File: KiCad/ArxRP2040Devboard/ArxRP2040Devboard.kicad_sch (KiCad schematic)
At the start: 14 parts, among them J1 USB_C_Receptacle_USB2.0_14P, U2 RP2040

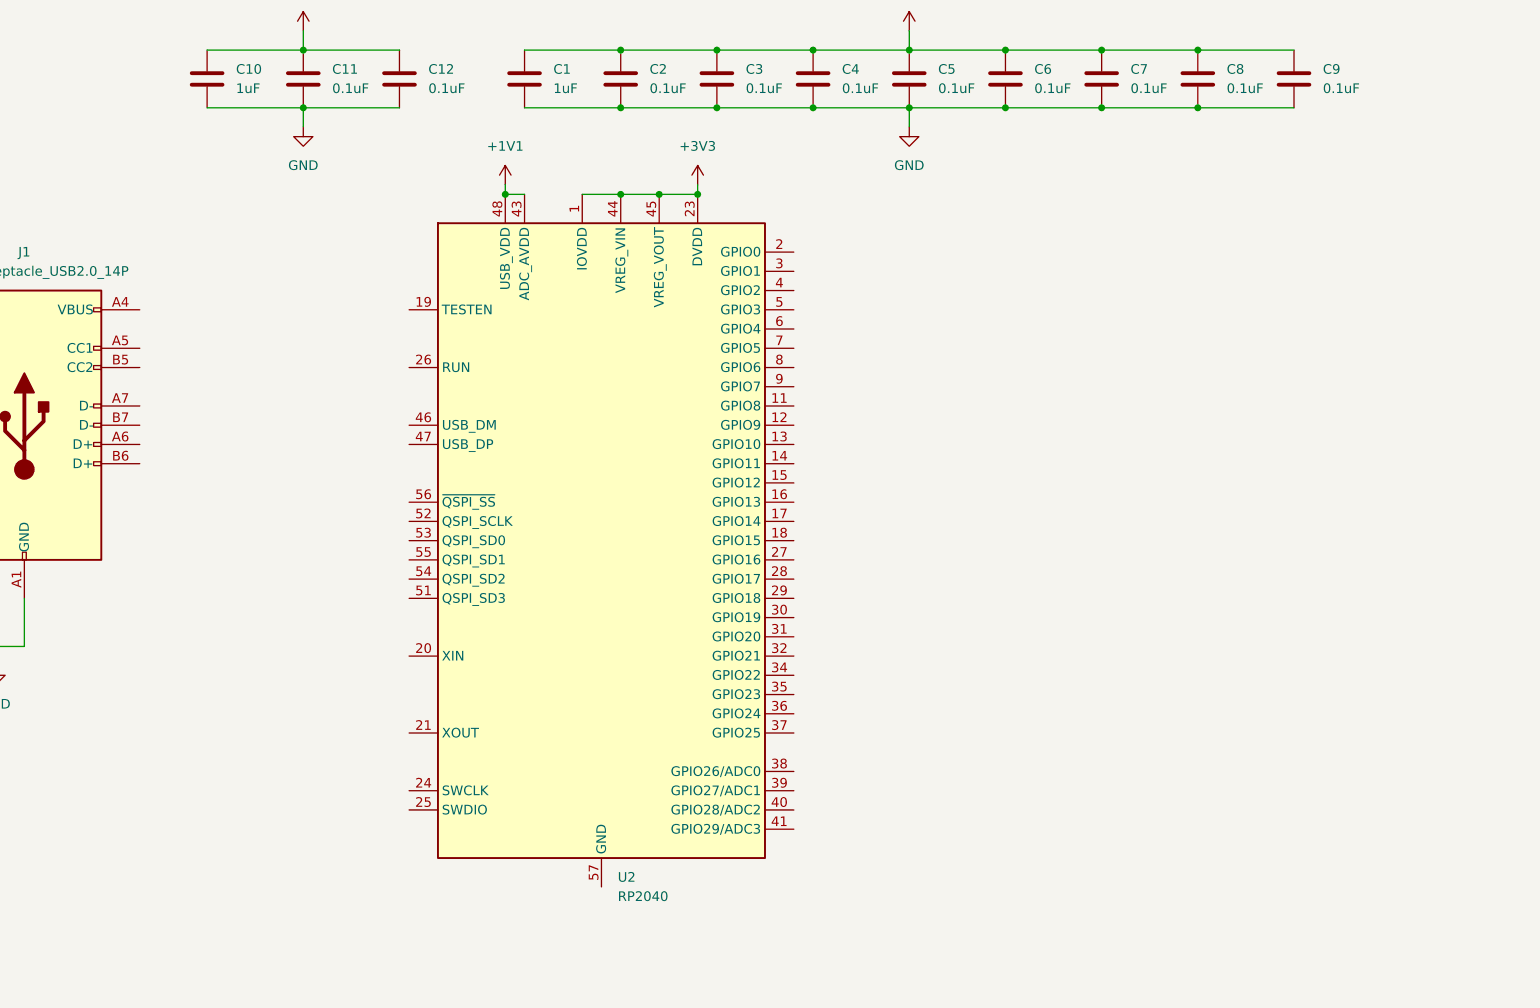
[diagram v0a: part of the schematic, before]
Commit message: More connections
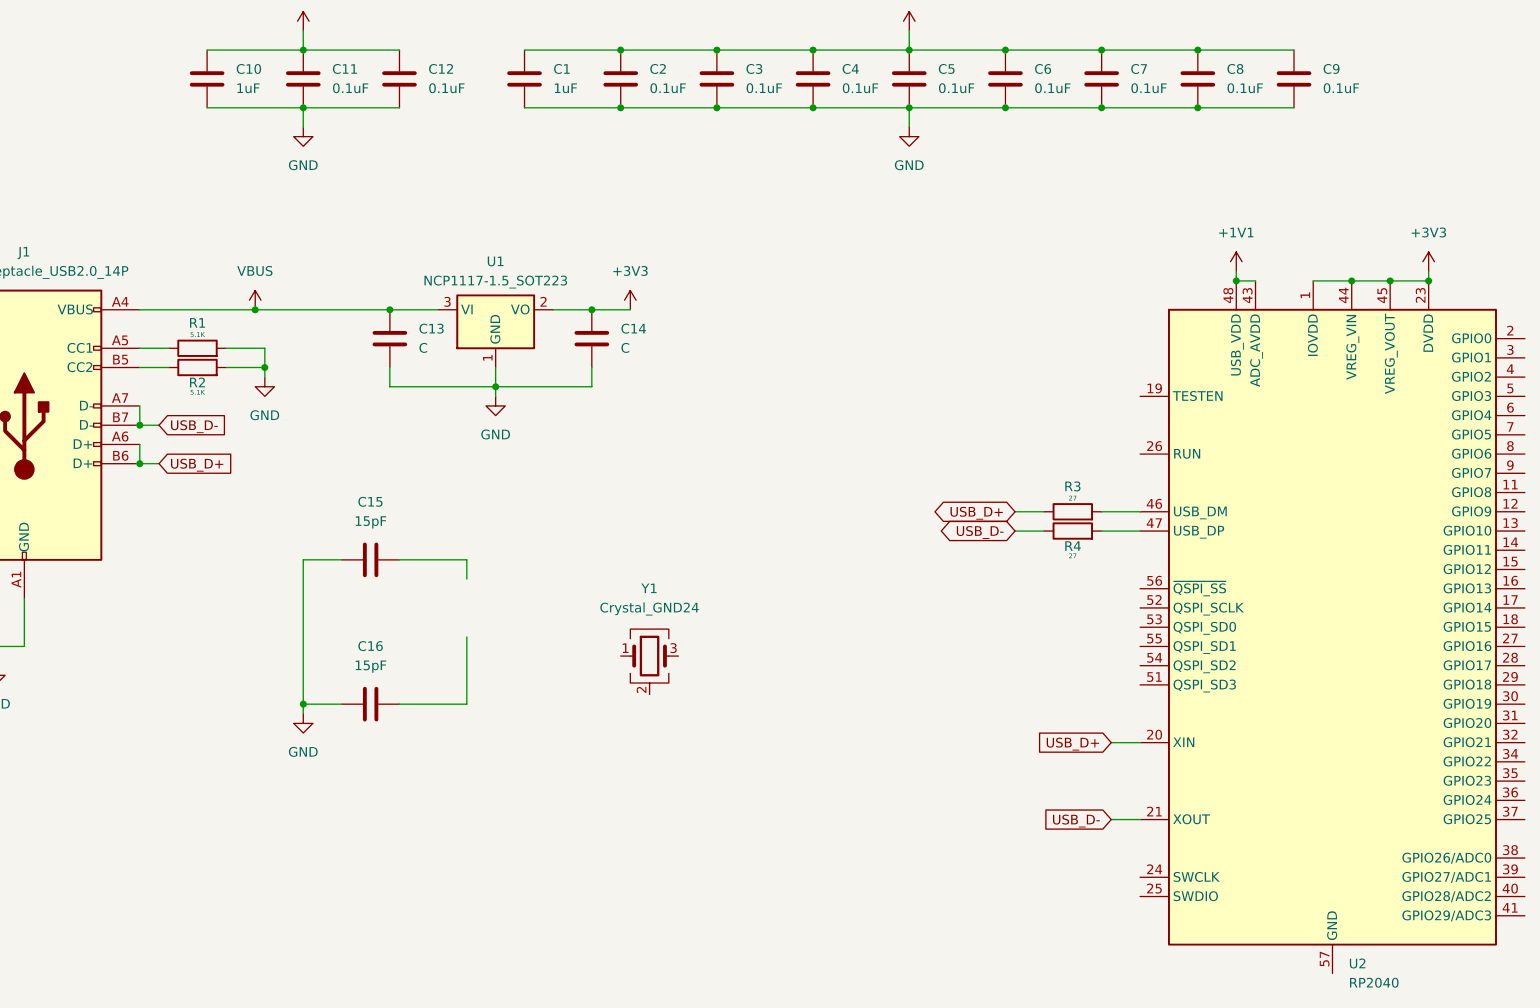
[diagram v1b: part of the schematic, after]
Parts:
- added C13, C14: C, symbol Device:C
- added C15, C16: 15pF, symbol Device:C
- added R1, R2: 5.1K, symbol Device:R
- added R3, R4: 27, symbol Device:R
- added U1: NCP1117-1.5_SOT223, Package_TO_SOT_SMD:SOT-223-3_TabPin2, symbol Regulator_Linear:NCP1117-1.5_SOT223
- added Y1: Crystal_GND24, symbol Device:Crystal_GND24
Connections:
- net +3V3: now also C14.1, U1.2 (VO)
- net GND: now also C13.2, C14.2, C15.1, C16.1, R1.2, R2.2, U1.1 (GND)
- net VBUS: now reaches J1.A4 (VBUS), J1.A9 (VBUS), J1.B4 (VBUS), J1.B9 (VBUS)
- net VBUS: now also C13.1, U1.3 (VI)
- net at J1.A5 (CC1): now also R1.1
- net USB_D+: now reaches J1.A6 (D+)
- net USB_D+: now also J1.B6 (D+), U2.20 (XIN), R3.1
- net USB_D-: now reaches J1.A7 (D-)
- net USB_D-: now also J1.B7 (D-), U2.21 (XOUT), R4.1
- net at J1.B5 (CC2): now also R2.1
- net at U2.46 (USB_DM): now also R3.2
- net at U2.47 (USB_DP): now also R4.2
- new net: Y1.2 (G), Y1.4 (G)
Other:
- moved on the sheet: U2

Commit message: KiCad wiring
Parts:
- added R5, R6: 1K, symbol kicadunlocked:R
- added R7: 10K, symbol kicadunlocked:R
- added SW1: SW_Push, symbol Switch:SW_Push
- added U3: W25Q128JVS, Package_SO:SOIC-8_5.3x5.3mm_P1.27mm, symbol Memory_Flash:W25Q128JVS
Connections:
- net +3V3: now also R7.1, U3.8 (VCC)
- net GND: now also U2.19 (TESTEN), U2.57 (GND), Y1.2 (G), Y1.4 (G), SW1.1, U3.4 (GND)
- net at C16.2: now also Y1.3
- net XIN: now reaches Y1.1
- net XIN: now also C15.2
- net GPIO8: now reaches U2.11 (GPIO8)
- net GPIO9: now reaches U2.12 (GPIO9)
- net GPIO10: now reaches U2.13 (GPIO10)
- net GPIO11: now reaches U2.14 (GPIO11)
- net GPIO12: now reaches U2.15 (GPIO12)
- net GPIO13: now reaches U2.16 (GPIO13)
- net GPIO14: now reaches U2.17 (GPIO14)
- net GPIO15: now reaches U2.18 (GPIO15)
- net GPIO0: now reaches U2.2 (GPIO0)
- net SWCLK: now reaches U2.24 (SWCLK)
- net SWDIO: now reaches U2.25 (SWDIO)
- net RUN: now reaches U2.26 (RUN)
- net GPIO16: now reaches U2.27 (GPIO16)
- net GPIO17: now reaches U2.28 (GPIO17)
- net GPIO18: now reaches U2.29 (GPIO18)
- net GPIO1: now reaches U2.3 (GPIO1)
- net GPIO19: now reaches U2.30 (GPIO19)
- net GPIO20: now reaches U2.31 (GPIO20)
- net GPIO21: now reaches U2.32 (GPIO21)
- net GPIO22: now reaches U2.34 (GPIO22)
- net GPIO23: now reaches U2.35 (GPIO23)
- net GPIO24: now reaches U2.36 (GPIO24)
- net GPIO25: now reaches U2.37 (GPIO25)
- net GPIO26_ADC0: now reaches U2.38 (GPIO26/ADC0)
- net GPIO26_ADC1: now reaches U2.39 (GPIO27/ADC1)
- net GPIO2: now reaches U2.4 (GPIO2)
- net GPIO26_ADC2: now reaches U2.40 (GPIO28/ADC2)
- net GPIO26_ADC3: now reaches U2.41 (GPIO29/ADC3)
- net GPIO3: now reaches U2.5 (GPIO3)
- net QSPI_D3: now reaches U2.51 (QSPI_SD3)
- net QSPI_D3: now also U3.7 (~{HOLD}/~{RESET}/IO_{3})
- net QSPI_SCLK: now reaches U2.52 (QSPI_SCLK)
- net QSPI_SCLK: now also U3.6 (CLK)
- net QSPI_D0: now reaches U2.53 (QSPI_SD0)
- net QSPI_D0: now also U3.5 (DI/IO_{0})
- net QSPI_D2: now reaches U2.54 (QSPI_SD2)
- net QSPI_D2: now also U3.3 (~{WP}/IO_{2})
- net QSPI_D1: now reaches U2.55 (QSPI_SD1)
- net QSPI_D1: now also U3.2 (DO/IO_{1})
- net QSPI_SS: now reaches U2.56 (~{QSPI_SS})
- net QSPI_SS: now also R6.2, R7.2, U3.1 (~{CS})
- net GPIO4: now reaches U2.6 (GPIO4)
- net GPIO5: now reaches U2.7 (GPIO5)
- net GPIO6: now reaches U2.8 (GPIO6)
- net GPIO7: now reaches U2.9 (GPIO7)
- new net: R6.1, SW1.2
- new net XOUT: R5.2
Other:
- moved on the sheet: C1, C10, C11, C12, C2, C3, C4, C5, C6, C7, C8, C9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

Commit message: wiring
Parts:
- added J2: Conn_01x03, symbol Connector_Generic:Conn_01x03
- added J3, J4: Conn_01x20, symbol Connector_Generic:Conn_01x20
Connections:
- net +3V3: now also J3.5 (Pin_5)
- net GND: now also J2.2 (Pin_2), J3.13 (Pin_13), J3.18 (Pin_18), J3.3 (Pin_3), J3.8 (Pin_8), J4.13 (Pin_13), J4.18 (Pin_18), J4.3 (Pin_3), J4.8 (Pin_8)
- net GPIO0: now also J4.1 (Pin_1)
- net GPIO1: now also J4.2 (Pin_2)
- net GPIO10: now also J4.14 (Pin_14)
- net GPIO11: now also J4.15 (Pin_15)
- net GPIO12: now also J4.16 (Pin_16)
- net GPIO13: now also J4.17 (Pin_17)
- net GPIO14: now also J4.19 (Pin_19)
- net GPIO15: now also J4.20 (Pin_20)
- net GPIO16: now also J3.20 (Pin_20)
- net GPIO17: now also J3.19 (Pin_19)
- net GPIO18: now also J3.17 (Pin_17)
- net GPIO19: now also J3.16 (Pin_16)
- net GPIO2: now also J4.4 (Pin_4)
- net GPIO20: now also J3.15 (Pin_15)
- net GPIO21: now also J3.14 (Pin_14)
- net GPIO22: now also J3.12 (Pin_12)
- net GPIO23: now also J3.10 (Pin_10)
- net GPIO24: now also J3.9 (Pin_9)
- net GPIO26_ADC0: now also J3.7 (Pin_7)
- net GPIO26_ADC1: now also J3.6 (Pin_6)
- net GPIO26_ADC2: now also J3.4 (Pin_4)
- net GPIO26_ADC3: now also J3.2 (Pin_2)
- net GPIO3: now also J4.5 (Pin_5)
- net GPIO4: now also J4.6 (Pin_6)
- net GPIO5: now also J4.7 (Pin_7)
- net GPIO6: now also J4.9 (Pin_9)
- net GPIO7: now also J4.10 (Pin_10)
- net GPIO8: now also J4.11 (Pin_11)
- net GPIO9: now also J4.12 (Pin_12)
- net RUN: now also J3.11 (Pin_11)
- net SWCLK: now also J2.1 (Pin_1)
- net SWDIO: now also J2.3 (Pin_3)
- net VBUS: now also J3.1 (Pin_1)
- net GPIO25: no longer names the net of U2.37 (GPIO25)
- no-connect marks 0 -> 1

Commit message: Schematic update
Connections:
- net at C16.2, Y1.3: now also R5.1
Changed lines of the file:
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@@
 	)
 	(junction
+		(at 105.41 118.11)
+		(diameter 0)
+		(color 0 0 0 0)
+	)
+	(junction
 		(at 294.64 120.65)
 		(diameter 0)
@@
 	(wire
 		(pts
+			(xy 105.41 118.11) (xy 114.3 118.11)
+		)
+		(stroke
+			(width 0)
+			(type default)
+		)
+	)
+	(wire
+		(pts
 			(xy 292.1 90.17) (xy 295.91 90.17)
 		)
@@
 	(wire
 		(pts
-			(xy 105.41 118.11) (xy 96.52 118.11)
+			(xy 96.52 118.11) (xy 105.41 118.11)
 		)
 		(stroke
@@
 		)
 	)
-	(global_label "GPIO26_ADC1"
-		(shape bidirectional)
-		(at 88.9 148.59 180)
-		(fields_autoplaced yes)
-		(effects
-			(font
-				(size 1.27 1.27)
-			)
-			(justify right)
-		)
-		(property "Intersheetrefs" "${INTERSHEET_REFS}"
-			(at 72.1035 148.59 0)
-			(hide yes)
-			(show_name no)
-			(do_not_autoplace no)
-			(effects
-				(font
-					(size 1.27 1.27)
-				)
-				(justify right)
-			)
-		)
-	)
 	(global_label "XIN"
 		(shape input)
@@
 		)
 	)
-	(global_label "GPIO26_ADC2"
-		(shape bidirectional)
-		(at 88.9 146.05 180)
-		(fields_autoplaced yes)
-		(effects
-			(font
-				(size 1.27 1.27)
-			)
-			(justify right)
-		)
-		(property "Intersheetrefs" "${INTERSHEET_REFS}"
-			(at 72.1035 146.05 0)
-			(hide yes)
-			(show_name no)
-			(do_not_autoplace no)
-			(effects
-				(font
-					(size 1.27 1.27)
-				)
-				(justify right)
-			)
-		)
-	)
 	(global_label "GPIO16"
 		(shape bidirectional)
@@
 		)
 	)
-	(global_label "GPIO26_ADC0"
-		(shape bidirectional)
-		(at 88.9 151.13 180)
-		(fields_autoplaced yes)
-		(effects
-			(font
-				(size 1.27 1.27)
-			)
-			(justify right)
-		)
-		(property "Intersheetrefs" "${INTERSHEET_REFS}"
-			(at 72.1035 151.13 0)
-			(hide yes)
-			(show_name no)
-			(do_not_autoplace no)
-			(effects
-				(font
-					(size 1.27 1.27)
-				)
-				(justify right)
-			)
-		)
-	)
 	(global_label "GPIO8"
 		(shape bidirectional)
@@
 			)
 		)
-	)
-	(global_label "GPIO26_ADC3"
-		(shape bidirectional)
-		(at 88.9 143.51 180)
-		(fields_autoplaced yes)
-		(effects
-			(font
-				(size 1.27 1.27)
-			)
-			(justify right)
-		)
-		(property "Intersheetrefs" "${INTERSHEET_REFS}"
-			(at 72.1035 143.51 0)
-			(hide yes)
-			(show_name no)
-			(do_not_autoplace no)
-			(effects
-				(font
-					(size 1.27 1.27)
-				)
-				(justify right)
-			)
-		)

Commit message: Add files via upload
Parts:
- C1, C10, C11, C12, C2, C3, C4, C5, C6, C7, C8, C9: footprint (none) -> Capacitor_SMD:C_0402_1005Metric
- C13, C14: value C -> 10uF; footprint (none) -> Capacitor_SMD:C_0201_0603Metric
- C15, C16: value 15pF -> 33pF; footprint (none) -> Capacitor_SMD:C_0402_1005Metric
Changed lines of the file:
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@@
 	)
 	(junction
+		(at 105.41 118.11)
+		(diameter 0)
+		(color 0 0 0 0)
+	)
+	(junction
 		(at 227.33 62.23)
 		(diameter 0)
@@
 	)
 	(junction
-		(at 105.41 118.11)
-		(diameter 0)
-		(color 0 0 0 0)
-	)
-	(junction
 		(at 294.64 120.65)
 		(diameter 0)
@@
 	(wire
 		(pts
+			(xy 105.41 118.11) (xy 114.3 118.11)
+		)
+		(stroke
+			(width 0)
+			(type default)
+		)
+	)
+	(wire
+		(pts
 			(xy 140.97 33.02) (xy 153.67 33.02)
 		)
@@
 	(wire
 		(pts
-			(xy 105.41 118.11) (xy 114.3 118.11)
-		)
-		(stroke
-			(width 0)
-			(type default)
-		)
-	)
-	(wire
-		(pts
 			(xy 292.1 90.17) (xy 295.91 90.17)
 		)
@@
 	(wire
 		(pts
-			(xy 96.52 118.11) (xy 105.41 118.11)
+			(xy 105.41 118.11) (xy 96.52 118.11)
 		)
 		(stroke
@@
 		)
 	)
+	(global_label "GPIO26_ADC1"
+		(shape bidirectional)
+		(at 88.9 148.59 180)
+		(fields_autoplaced yes)
+		(effects
+			(font
+				(size 1.27 1.27)
+			)
+			(justify right)
+		)
+		(property "Intersheetrefs" "${INTERSHEET_REFS}"
+			(at 72.1035 148.59 0)
+			(hide yes)
+			(show_name no)
+			(do_not_autoplace no)
+			(effects
+				(font
+					(size 1.27 1.27)
+				)
+				(justify right)
+			)
+		)
+	)
 	(global_label "XIN"
 		(shape input)
@@
 		)
 	)
+	(global_label "GPIO26_ADC2"
+		(shape bidirectional)
+		(at 88.9 146.05 180)
+		(fields_autoplaced yes)
+		(effects
+			(font
+				(size 1.27 1.27)
+			)
+			(justify right)
+		)
+		(property "Intersheetrefs" "${INTERSHEET_REFS}"
+			(at 72.1035 146.05 0)
+			(hide yes)
+			(show_name no)
+			(do_not_autoplace no)
+			(effects
+				(font
+					(size 1.27 1.27)
+				)
+				(justify right)
+			)
+		)
+	)
 	(global_label "GPIO16"
 		(shape bidirectional)
@@
 		)
 	)
+	(global_label "GPIO26_ADC0"
+		(shape bidirectional)
+		(at 88.9 151.13 180)
+		(fields_autoplaced yes)
+		(effects
+			(font
+				(size 1.27 1.27)
+			)
+			(justify right)
+		)
+		(property "Intersheetrefs" "${INTERSHEET_REFS}"
+			(at 72.1035 151.13 0)
+			(hide yes)
+			(show_name no)
+			(do_not_autoplace no)
+			(effects
+				(font
+					(size 1.27 1.27)
+				)
+				(justify right)
+			)
+		)
+	)
 	(global_label "GPIO8"
 		(shape bidirectional)
@@
 		)
 	)
+	(global_label "GPIO26_ADC3"
+		(shape bidirectional)
+		(at 88.9 143.51 180)
+		(fields_autoplaced yes)
+		(effects
+			(font
+				(size 1.27 1.27)
+			)
+			(justify right)
+		)
+		(property "Intersheetrefs" "${INTERSHEET_REFS}"
+			(at 72.1035 143.51 0)
+			(hide yes)
+			(show_name no)
+			(do_not_autoplace no)
+			(effects
+				(font
+					(size 1.27 1.27)
+				)
+				(justify right)
+			)
+		)
+	)
 	(symbol
 		(lib_id "Connector_Generic:Conn_01x03")
@@
 			)
 		)
-		(property "Value" "15pF"
+		(property "Value" "33pF"
 			(at 92.71 113.03 90)
 			(show_name no)
@@
 			)
 		)
-		(property "Footprint" ""
+		(property "Footprint" "Capacitor_SMD:C_0402_1005Metric"
 			(at 96.52 117.1448 0)
 			(hide yes)
@@
 			)
 		)
-		(property "Footprint" ""
+		(property "Footprint" "Capacitor_SMD:C_0402_1005Metric"
 			(at 129.2352 33.02 0)
 			(hide yes)
@@
 			)
 		)
-		(property "Footprint" ""
+		(property "Footprint" "Capacitor_SMD:C_0402_1005Metric"
 			(at 260.0452 33.02 0)
 			(hide yes)
@@
 			)
 		)
-		(property "Value" "C"
+		(property "Value" "10uF"
 			(at 99.06 71.1199 0)
 			(show_name no)
@@
 			)
 		)
-		(property "Footprint" ""
+		(property "Footprint" "Capacitor_SMD:C_0201_0603Metric"
 			(at 96.2152 73.66 0)
 			(hide yes)
@@
 			)
 		)
-		(property "Footprint" ""
+		(property "Footprint" "Capacitor_SMD:C_0402_1005Metric"
 			(at 221.9452 33.02 0)
 			(hide yes)
@@
 			)
 		)
-		(property "Footprint" ""
+		(property "Footprint" "Capacitor_SMD:C_0402_1005Metric"
 			(at 209.2452 33.02 0)
 			(hide yes)
@@
 			)
 		)
-		(property "Footprint" ""
+		(property "Footprint" "Capacitor_SMD:C_0402_1005Metric"
 			(at 196.5452 33.02 0)
 			(hide yes)
@@
 			)
 		)
-		(property "Footprint" ""
+		(property "Footprint" "Capacitor_SMD:C_0402_1005Metric"
 			(at 272.7452 33.02 0)
 			(hide yes)
@@
 			)
 		)
-		(property "Footprint" ""
+		(property "Footprint" "Capacitor_SMD:C_0402_1005Metric"
 			(at 234.6452 33.02 0)
 			(hide yes)
@@
 			)
 		)
-		(property "Footprint" ""
+		(property "Footprint" "Capacitor_SMD:C_0402_1005Metric"
 			(at 247.3452 33.02 0)
 			(hide yes)
@@
 			)
 		)
-		(property "Value" "15pF"
+		(property "Value" "33pF"
 			(at 92.71 93.98 90)
 			(show_name no)
@@
 			)
 		)
-		(property "Footprint" ""
+		(property "Footprint" "Capacitor_SMD:C_0402_1005Metric"
 			(at 96.52 98.0948 0)
 			(hide yes)
@@
 			)
 		)
-		(property "Footprint" ""
+		(property "Footprint" "Capacitor_SMD:C_0402_1005Metric"
 			(at 154.6352 33.02 0)
 			(hide yes)
@@
 			)
 		)
-		(property "Footprint" ""
+		(property "Footprint" "Capacitor_SMD:C_0402_1005Metric"
 			(at 171.1452 33.02 0)
 			(hide yes)
@@
 			)
 		)
-		(property "Footprint" ""
+		(property "Footprint" "Capacitor_SMD:C_0402_1005Metric"
 			(at 141.9352 33.02 0)
 			(hide yes)
@@
 			)
 		)
-		(property "Value" "C"
+		(property "Value" "10uF"
 			(at 125.73 71.1199 0)
 			(show_name no)
@@
 			)
 		)
-		(property "Footprint" ""
+		(property "Footprint" "Capacitor_SMD:C_0201_0603Metric"
 			(at 122.8852 73.66 0)
 			(hide yes)
@@
 			)
 		)
-		(property "Footprint" ""
+		(property "Footprint" "Capacitor_SMD:C_0402_1005Metric"
 			(at 183.8452 33.02 0)
 			(hide yes)

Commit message: schematics
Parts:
- removed U1: NCP1117-1.5_SOT223, Package_TO_SOT_SMD:SOT-223-3_TabPin2, symbol Regulator_Linear:NCP1117-1.5_SOT223
- removed U3: W25Q128JVS, Package_SO:SOIC-8_5.3x5.3mm_P1.27mm, symbol Memory_Flash:W25Q128JVS
- added C17: 0.1uF, Capacitor_SMD:C_0402_1005Metric, symbol Device:C
- added U1: MCP1700x-330xxTT, Package_TO_SOT_SMD:SOT-23, symbol Regulator_Linear:MCP1700x-330xxTT
- added U4: W25Q16JVZPIQ, Package_SON:Winbond_USON-8-1EP_3x2mm_P0.5mm_EP0.2x1.6mm, symbol W25Q16JVZPIQ:W25Q16JVZPIQ
- C13, C14: footprint Capacitor_SMD:C_0201_0603Metric -> Capacitor_SMD:C_0603_1608Metric
- J1: footprint (none) -> Connector_USB:USB_C_Receptacle_HRO_TYPE-C-31-M-12
- J2: footprint (none) -> Connector_PinHeader_2.54mm:PinHeader_1x03_P2.54mm_Vertical
- J3, J4: footprint (none) -> Connector_PinHeader_2.54mm:PinHeader_1x20_P2.54mm_Vertical
- R1, R2, R3, R4, R5, R6, R7: footprint (none) -> Resistor_SMD:R_0402_1005Metric
- SW1: footprint (none) -> Button_Switch_SMD:SW_Push_SPST_NO_Alps_SKRK
- Y1: footprint (none) -> Crystal:Crystal_SMD_3225-4Pin_3.2x2.5mm_HandSoldering
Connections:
- net +3V3: now also C17.1, U1.2 (VO), U4.8 (VCC)
- net GND: now also C17.2, U1.1 (GND)
- net QSPI_D0: now also U4.5 (DI(IO0))
- net QSPI_D1: now also U4.2 (DO(IO1))
- net QSPI_D2: now also U4.3 (~{WP}(IO2))
- net QSPI_D3: now also U4.7 (~{HOLD}/RESET(IO3))
- net QSPI_SCLK: now also U4.6 (CLK)
- net QSPI_SS: now also U4.1 (~{CS})
- net USB_D+: now also R4.1; no longer R3.1, U2.20 (XIN)
- net USB_D-: now also R3.1; no longer R4.1, U2.21 (XOUT)
- net VBUS: now also U1.3 (VI)
- net XIN: now also U2.20 (XIN)
- net XOUT: now also U2.21 (XOUT)
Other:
- moved on the sheet: C1, C10, C11, C12, C13, C14, C15, C16, C2, C3, C4, C5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

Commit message: PCB Designed!!!!!
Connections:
- net +1V1: now also C10.1, C11.1, C12.1, U2.23 (DVDD), U2.45 (VREG_VOUT), U2.50 (DVDD); no longer U2.43 (ADC_AVDD), U2.48 (USB_VDD)
- net +3V3: now also U2.43 (ADC_AVDD), U2.48 (USB_VDD); no longer C10.1, C11.1, C12.1, U2.23 (DVDD), U2.45 (VREG_VOUT), U2.50 (DVDD)
- net GND: now also U4.4 (GND)
- net XIN: now also Y1.3; no longer Y1.1
- net at C16.2, R5.1: now also Y1.1; no longer Y1.3
- no-connect marks 1 -> 2
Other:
- moved on the sheet: R7, Y1
